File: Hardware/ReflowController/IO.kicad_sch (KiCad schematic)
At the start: 18 parts, among them U5 SZNUD3124DMT1G, U6 VNQ5160K-E

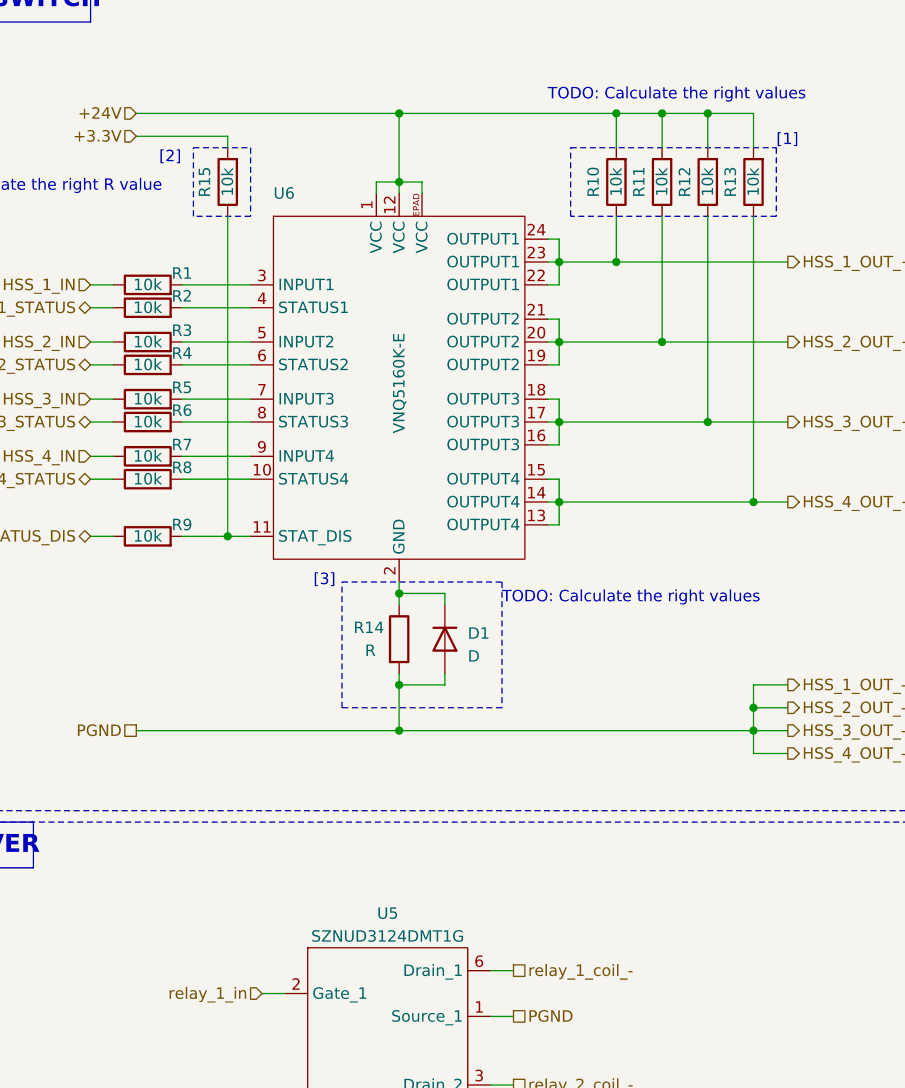
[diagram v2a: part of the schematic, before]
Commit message: finished the io control for the pcb, need to define what is the best way for a remote keypad
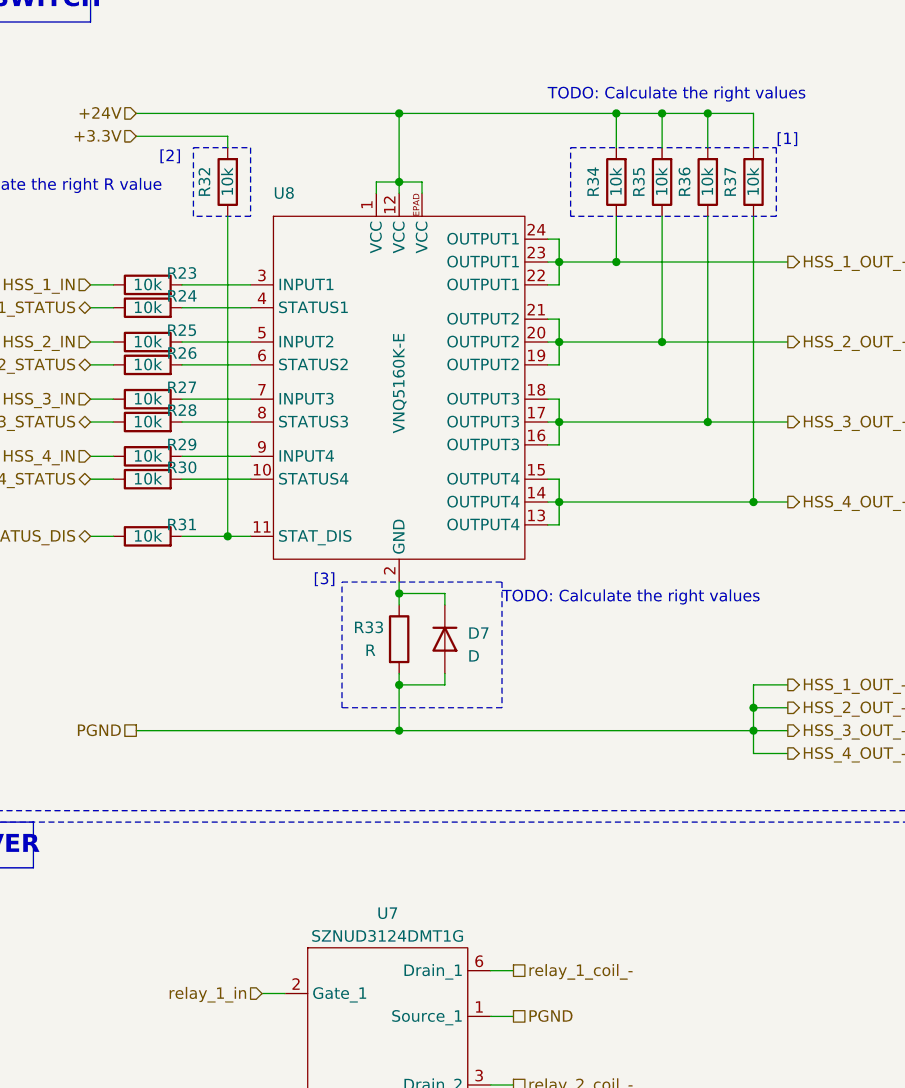
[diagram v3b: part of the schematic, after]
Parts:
- renumbered D1 to D7, R1 to R23, R2 to R24, R3 to R25, R4 to R26, R5 to R27, R6 to R28, R7 to R29, R8 to R30, R9 to R31, R15 to R32, R14 to R33, R10 to R34, R11 to R35, R12 to R36, R13 to R37, U5 to U7, U6 to U8
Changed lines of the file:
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@@
   (symbol (lib_id "Device:R") (at 48.26 59.69 90) (unit 1)
     (in_bom yes) (on_board yes) (dnp no)
-    (property "Reference" "R5" (at 52.07 58.42 90)
+    (property "Reference" "R27" (at 52.07 58.42 90)
       (effects (font (size 1.27 1.27)))
     )
@@
       (project "ReflowController"
         (path "/2394cc2a-b9b0-4c0b-be11-1fc6085b0d5c/7eb2c85f-b182-4872-bcd3-2e9396dd27ee"
-          (reference "R5") (unit 1)
+          (reference "R27") (unit 1)
         )
       )
@@
   (symbol (lib_id "190_active_high_side_switches:VNQ5160K") (at 76.2 57.15 0) (unit 1)
     (in_bom yes) (on_board yes) (dnp no)
-    (property "Reference" "U6" (at 62.23 36.83 0)
+    (property "Reference" "U8" (at 62.23 36.83 0)
       (effects (font (size 1.27 1.27)) (justify left))
     )
@@
       (project "ReflowController"
         (path "/2394cc2a-b9b0-4c0b-be11-1fc6085b0d5c/7eb2c85f-b182-4872-bcd3-2e9396dd27ee"
-          (reference "U6") (unit 1)
+          (reference "U8") (unit 1)
         )
       )
@@
   (symbol (lib_id "Device:R") (at 57.15 35.56 180) (unit 1)
     (in_bom yes) (on_board yes) (dnp no)
-    (property "Reference" "R15" (at 54.61 35.56 90)
+    (property "Reference" "R32" (at 54.61 35.56 90)
       (effects (font (size 1.27 1.27)))
     )
@@
       (project "ReflowController"
         (path "/2394cc2a-b9b0-4c0b-be11-1fc6085b0d5c/7eb2c85f-b182-4872-bcd3-2e9396dd27ee"
-          (reference "R15") (unit 1)
+          (reference "R32") (unit 1)
         )
       )
@@
   (symbol (lib_id "Device:R") (at 48.26 49.53 90) (unit 1)
     (in_bom yes) (on_board yes) (dnp no)
-    (property "Reference" "R2" (at 52.07 48.26 90)
+    (property "Reference" "R24" (at 52.07 48.26 90)
       (effects (font (size 1.27 1.27)))
     )
@@
       (project "ReflowController"
         (path "/2394cc2a-b9b0-4c0b-be11-1fc6085b0d5c/7eb2c85f-b182-4872-bcd3-2e9396dd27ee"
-          (reference "R2") (unit 1)
+          (reference "R24") (unit 1)
         )
       )
@@
   (symbol (lib_id "Device:R") (at 48.26 55.88 90) (unit 1)
     (in_bom yes) (on_board yes) (dnp no)
-    (property "Reference" "R4" (at 52.07 54.61 90)
+    (property "Reference" "R26" (at 52.07 54.61 90)
       (effects (font (size 1.27 1.27)))
     )
@@
       (project "ReflowController"
         (path "/2394cc2a-b9b0-4c0b-be11-1fc6085b0d5c/7eb2c85f-b182-4872-bcd3-2e9396dd27ee"
-          (reference "R4") (unit 1)
+          (reference "R26") (unit 1)
         )
       )
@@
   (symbol (lib_id "Device:D") (at 81.28 86.36 270) (unit 1)
     (in_bom yes) (on_board yes) (dnp no) (fields_autoplaced)
-    (property "Reference" "D1" (at 83.82 85.725 90)
+    (property "Reference" "D7" (at 83.82 85.725 90)
       (effects (font (size 1.27 1.27)) (justify left))
     )
@@
       (project "ReflowController"
         (path "/2394cc2a-b9b0-4c0b-be11-1fc6085b0d5c/7eb2c85f-b182-4872-bcd3-2e9396dd27ee"
-          (reference "D1") (unit 1)
+          (reference "D7") (unit 1)
         )
       )
@@
   (symbol (lib_id "Device:R") (at 48.26 46.99 90) (unit 1)
     (in_bom yes) (on_board yes) (dnp no)
-    (property "Reference" "R1" (at 52.07 45.72 90)
+    (property "Reference" "R23" (at 52.07 45.72 90)
       (effects (font (size 1.27 1.27)))
     )
@@
       (project "ReflowController"
         (path "/2394cc2a-b9b0-4c0b-be11-1fc6085b0d5c/7eb2c85f-b182-4872-bcd3-2e9396dd27ee"
-          (reference "R1") (unit 1)
+          (reference "R23") (unit 1)
         )
       )
@@
   (symbol (lib_id "Device:R") (at 76.2 86.36 0) (unit 1)
     (in_bom yes) (on_board yes) (dnp no)
-    (property "Reference" "R14" (at 71.12 85.09 0)
+    (property "Reference" "R33" (at 71.12 85.09 0)
       (effects (font (size 1.27 1.27)) (justify left))
     )
@@
       (project "ReflowController"
         (path "/2394cc2a-b9b0-4c0b-be11-1fc6085b0d5c/7eb2c85f-b182-4872-bcd3-2e9396dd27ee"
-          (reference "R14") (unit 1)
+          (reference "R33") (unit 1)
         )
       )
@@
   (symbol (lib_id "Device:R") (at 105.41 35.56 180) (unit 1)
     (in_bom yes) (on_board yes) (dnp no)
-    (property "Reference" "R11" (at 102.87 35.56 90)
+    (property "Reference" "R35" (at 102.87 35.56 90)
       (effects (font (size 1.27 1.27)))
     )
@@
       (project "ReflowController"
         (path "/2394cc2a-b9b0-4c0b-be11-1fc6085b0d5c/7eb2c85f-b182-4872-bcd3-2e9396dd27ee"
-          (reference "R11") (unit 1)
+          (reference "R35") (unit 1)
         )
       )
@@
   (symbol (lib_id "Device:R") (at 48.26 66.04 90) (unit 1)
     (in_bom yes) (on_board yes) (dnp no)
-    (property "Reference" "R7" (at 52.07 64.77 90)
+    (property "Reference" "R29" (at 52.07 64.77 90)
       (effects (font (size 1.27 1.27)))
     )
@@
       (project "ReflowController"
         (path "/2394cc2a-b9b0-4c0b-be11-1fc6085b0d5c/7eb2c85f-b182-4872-bcd3-2e9396dd27ee"
-          (reference "R7") (unit 1)
+          (reference "R29") (unit 1)
         )
       )
@@
   (symbol (lib_id "Device:R") (at 110.49 35.56 180) (unit 1)
     (in_bom yes) (on_board yes) (dnp no)
-    (property "Reference" "R12" (at 107.95 35.56 90)
+    (property "Reference" "R36" (at 107.95 35.56 90)
       (effects (font (size 1.27 1.27)))
     )
@@
       (project "ReflowController"
         (path "/2394cc2a-b9b0-4c0b-be11-1fc6085b0d5c/7eb2c85f-b182-4872-bcd3-2e9396dd27ee"
-          (reference "R12") (unit 1)
+          (reference "R36") (unit 1)
         )
       )
@@
   (symbol (lib_id "180_active_driver_relay:SZNUD3124DMT1G") (at 74.93 132.08 0) (unit 1)
     (in_bom yes) (on_board yes) (dnp no) (fields_autoplaced)
-    (property "Reference" "U5" (at 74.93 116.84 0)
+    (property "Reference" "U7" (at 74.93 116.84 0)
       (effects (font (size 1.27 1.27)))
     )
@@
       (project "ReflowController"
         (path "/2394cc2a-b9b0-4c0b-be11-1fc6085b0d5c/7eb2c85f-b182-4872-bcd3-2e9396dd27ee"
-          (reference "U5") (unit 1)
+          (reference "U7") (unit 1)
         )
       )
@@
   (symbol (lib_id "Device:R") (at 100.33 35.56 180) (unit 1)
     (in_bom yes) (on_board yes) (dnp no)
-    (property "Reference" "R10" (at 97.79 35.56 90)
+    (property "Reference" "R34" (at 97.79 35.56 90)
       (effects (font (size 1.27 1.27)))
     )
@@
       (project "ReflowController"
         (path "/2394cc2a-b9b0-4c0b-be11-1fc6085b0d5c/7eb2c85f-b182-4872-bcd3-2e9396dd27ee"
-          (reference "R10") (unit 1)
+          (reference "R34") (unit 1)
         )
       )
@@
   (symbol (lib_id "Device:R") (at 115.57 35.56 180) (unit 1)
     (in_bom yes) (on_board yes) (dnp no)
-    (property "Reference" "R13" (at 113.03 35.56 90)
+    (property "Reference" "R37" (at 113.03 35.56 90)
       (effects (font (size 1.27 1.27)))
     )
@@
       (project "ReflowController"
         (path "/2394cc2a-b9b0-4c0b-be11-1fc6085b0d5c/7eb2c85f-b182-4872-bcd3-2e9396dd27ee"
-          (reference "R13") (unit 1)
+          (reference "R37") (unit 1)
         )
       )
@@
   (symbol (lib_id "Device:R") (at 48.26 74.93 90) (unit 1)
     (in_bom yes) (on_board yes) (dnp no)
-    (property "Reference" "R9" (at 52.07 73.66 90)
+    (property "Reference" "R31" (at 52.07 73.66 90)
       (effects (font (size 1.27 1.27)))
     )
@@
       (project "ReflowController"
         (path "/2394cc2a-b9b0-4c0b-be11-1fc6085b0d5c/7eb2c85f-b182-4872-bcd3-2e9396dd27ee"
-          (reference "R9") (unit 1)
+          (reference "R31") (unit 1)
         )
       )
@@
   (symbol (lib_id "Device:R") (at 48.26 62.23 90) (unit 1)
     (in_bom yes) (on_board yes) (dnp no)
-    (property "Reference" "R6" (at 52.07 60.96 90)
+    (property "Reference" "R28" (at 52.07 60.96 90)
       (effects (font (size 1.27 1.27)))
     )
@@
       (project "ReflowController"
         (path "/2394cc2a-b9b0-4c0b-be11-1fc6085b0d5c/7eb2c85f-b182-4872-bcd3-2e9396dd27ee"
-          (reference "R6") (unit 1)
+          (reference "R28") (unit 1)
         )
       )
@@
   (symbol (lib_id "Device:R") (at 48.26 53.34 90) (unit 1)
     (in_bom yes) (on_board yes) (dnp no)
-    (property "Reference" "R3" (at 52.07 52.07 90)
+    (property "Reference" "R25" (at 52.07 52.07 90)
       (effects (font (size 1.27 1.27)))
     )
@@
       (project "ReflowController"
         (path "/2394cc2a-b9b0-4c0b-be11-1fc6085b0d5c/7eb2c85f-b182-4872-bcd3-2e9396dd27ee"
-          (reference "R3") (unit 1)
+          (reference "R25") (unit 1)
         )
       )
@@
   (symbol (lib_id "Device:R") (at 48.26 68.58 90) (unit 1)
     (in_bom yes) (on_board yes) (dnp no)
-    (property "Reference" "R8" (at 52.07 67.31 90)
+    (property "Reference" "R30" (at 52.07 67.31 90)
       (effects (font (size 1.27 1.27)))
     )
@@
       (project "ReflowController"
         (path "/2394cc2a-b9b0-4c0b-be11-1fc6085b0d5c/7eb2c85f-b182-4872-bcd3-2e9396dd27ee"
-          (reference "R8") (unit 1)
-        )
-      )
+          (reference "R30") (unit 1)
+        )
+      )

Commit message: Wrking with edwin on the hwole schematic
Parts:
- removed R32: 10k, Resistor_SMD:R_0603_1608Metric_Pad0.98x0.95mm_HandSolder, symbol Device:R
- added C4 (x2): 0.1uF, Capacitor_SMD:C_0603_1608Metric_Pad1.08x0.95mm_HandSolder, symbol Device:C
- added D8, D9: RSFJL, Diode_SMD:D_SMA_Handsoldering, symbol Device:D
- added NT34, NT35: NetTie_2, NetTie:NetTie-2_SMD_Pad2.0mm, symbol Device:NetTie_2
- added R12: 4.7K, Resistor_SMD:R_0603_1608Metric_Pad0.98x0.95mm_HandSolder, symbol Device:R
- D7: value D -> RSFJL; footprint (none) -> Diode_SMD:D_SMA_Handsoldering; disti (none) -> digikey; disti_no (none) -> 1801-RSFJLTR-ND; man (none) -> taiwan semi; man_no (none) -> RSFJL; now not fitted; now left out of the parts list
- R33: value R -> 0R; footprint (none) -> Resistor_SMD:R_1206_3216Metric; Field7 (none) -> 13-RC1206FR-134K7LTR-ND; disti (none) -> digikey; man (none) -> yageo; man_no (none) -> RC1206FR-134K7L
- R34, R35, R36, R37: now not fitted; now left out of the parts list
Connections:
- net +24V: now also C4.1, C4.1, NT34.1, NT35.1
- net HSS_1_OUT_-: now also D7.1 (K), C4.2, C4.2; no longer D7.2 (A)
- net relay_1_coil_-: now also D8.2 (A)
- net relay_2_coil_-: now also D9.2 (A)
- net at R31.2, U8.11 (STAT_DIS): now also R12.2
- net at R33.1, U8.2 (GND): now also D7.2 (A); no longer D7.1 (K)
- new net +3.3VD: R12.1
- new net relay_1_coil_+: D8.1 (K), NT34.2
- new net relay_2_coil_+: D9.1 (K), NT35.2
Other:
- note added: "[1] To be used if Open-load detection in off-state is needed"
- note added: "[3] To be used if GND protection network against reverse voltag For Reverse Battery voltage protection repace the 0 Ohm with 4k7 Ohm and populate the Diode"
- note removed: "TODO: Calculate the right R value"
- note removed: "[1] : To be used if Open-load detection in off-state is needed"
- note removed: "[2]"
- note removed: "[3] : To be used if GND protection network against reverse voltage"
- moved on the sheet: R23, R24, R25, R26, R27, R28, R29, R30, R31, R33, U7, U8

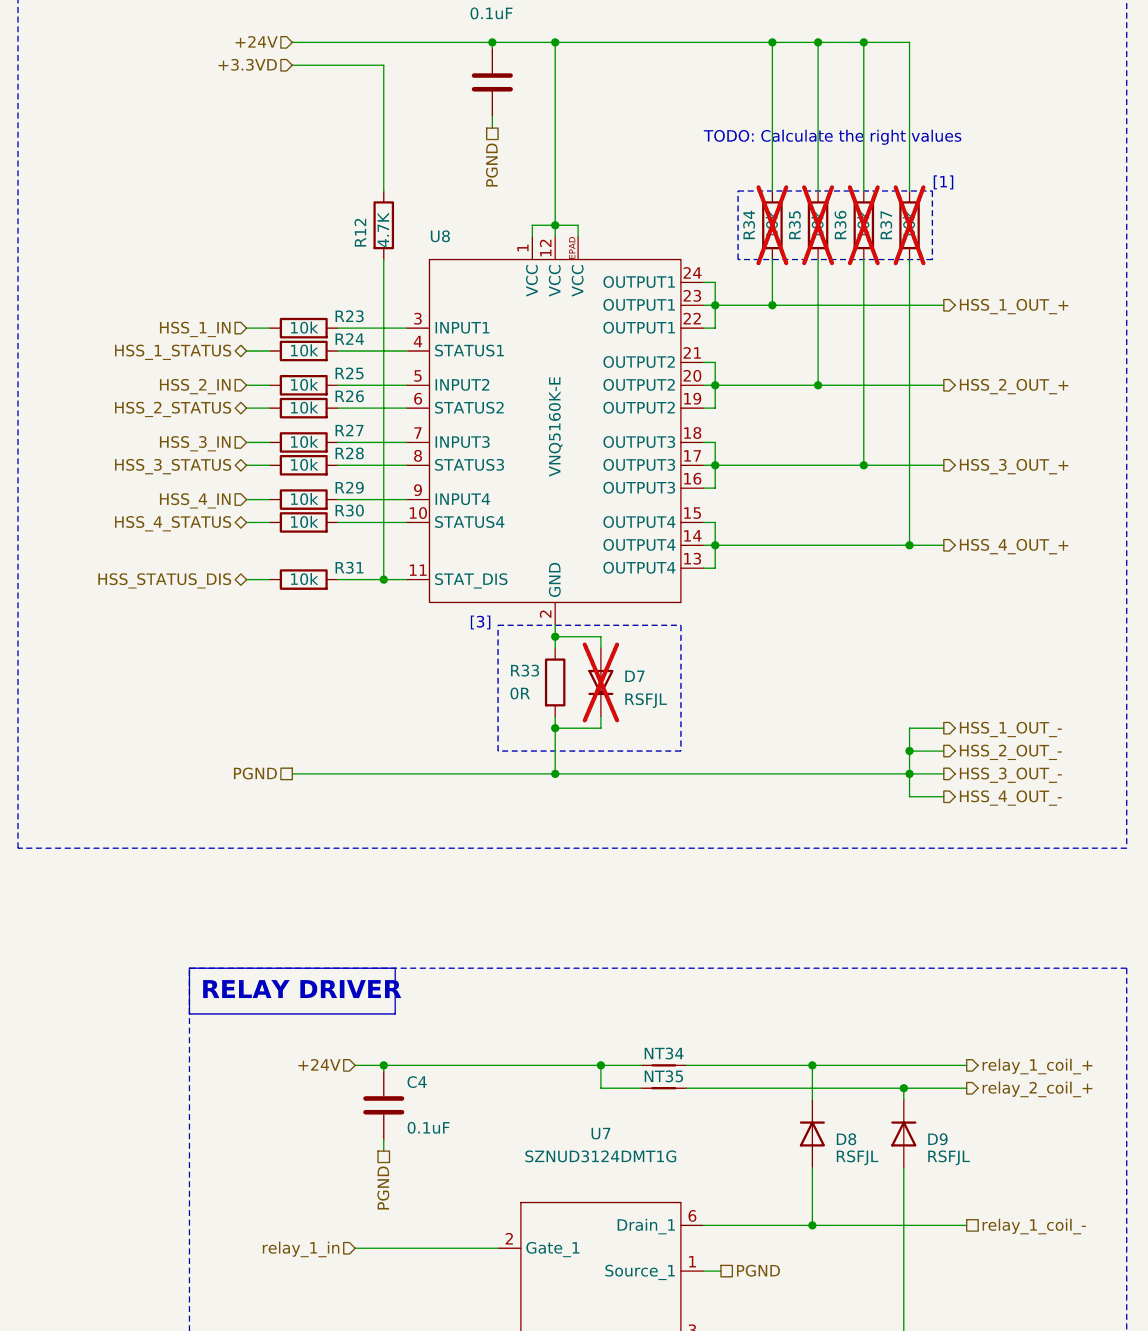
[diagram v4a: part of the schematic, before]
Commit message: Finished the desing of the PSUand started with the PCB TODO: missing fuse find a solution
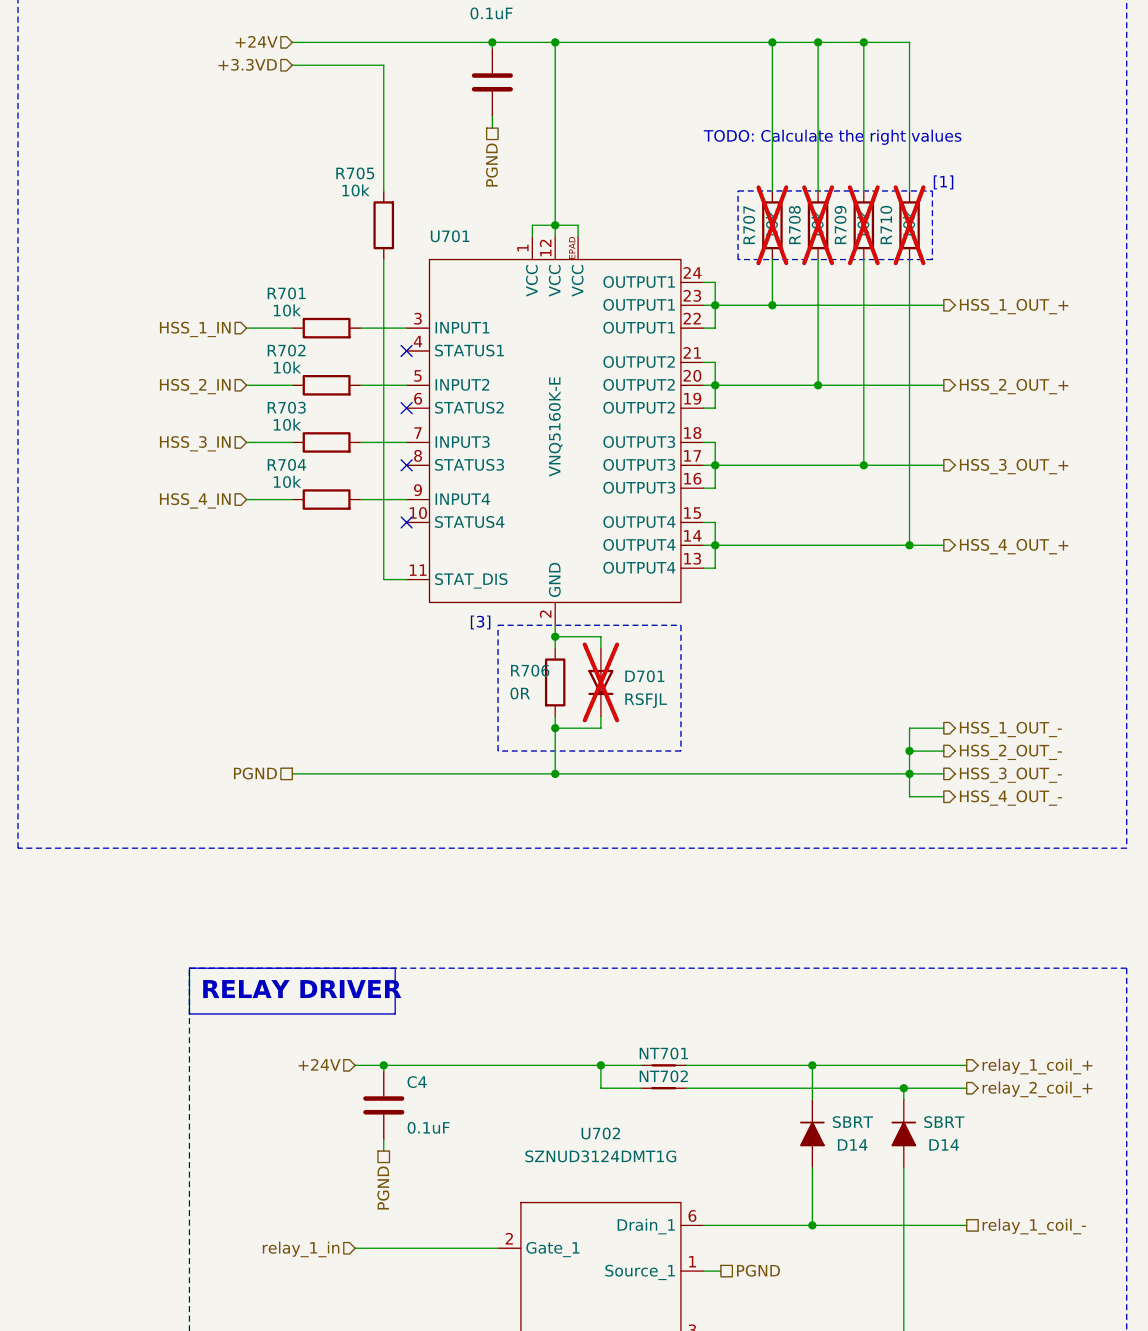
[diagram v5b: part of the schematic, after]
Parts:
- removed D8, D9: RSFJL, Diode_SMD:D_SMA_Handsoldering, symbol Device:D
- removed R12: 4.7K, Resistor_SMD:R_0603_1608Metric_Pad0.98x0.95mm_HandSolder, symbol Device:R
- removed R24, R26, R28, R30, R31: 10k, Resistor_SMD:R_0603_1608Metric_Pad0.98x0.95mm_HandSolder, symbol Device:R
- added D14 (x2): SBRT, Diode_SMD:D_SMA_Handsoldering, symbol Ampli50W-rescue:D_ALT
- added R705: 10k, Resistor_SMD:R_0603_1608Metric_Pad0.98x0.95mm_HandSolder, symbol Device:R
- renumbered D7 to D701, NT34 to NT701, NT35 to NT702, R23 to R701, R25 to R702, R27 to R703, R29 to R704, R33 to R706, R34 to R707, R35 to R708, R36 to R709, R37 to R710, U8 to U701, U7 to U702
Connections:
- net +3.3VD: now also R705.2
- net relay_1_coil_+: now also D14.1 (K)
- net relay_1_coil_-: now also D14.2 (A)
- net relay_2_coil_+: now also D14.1 (K)
- net relay_2_coil_-: now also D14.2 (A)
- net at U701.11 (STAT_DIS): now also R705.1
- no-connect marks 0 -> 4
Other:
- moved on the sheet: R701, R702, R703, R704
